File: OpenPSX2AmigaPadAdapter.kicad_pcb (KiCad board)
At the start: 2 copper layers, 58.9 x 44.2 mm, 42 parts, among them J1 TO_PSX_PAD, J2 DB9_F, J3 CONN_FTDI, J4 CONN_ICSP, J99 OSHW_LOGO, Q1 BSS138, Q2 BSS138, Q3 BSS138, Q4 BSS138, SW1 RESET, U1 ATmega328P-AU, U2 LM1117-3.3, Y1 16M, Y2 16M

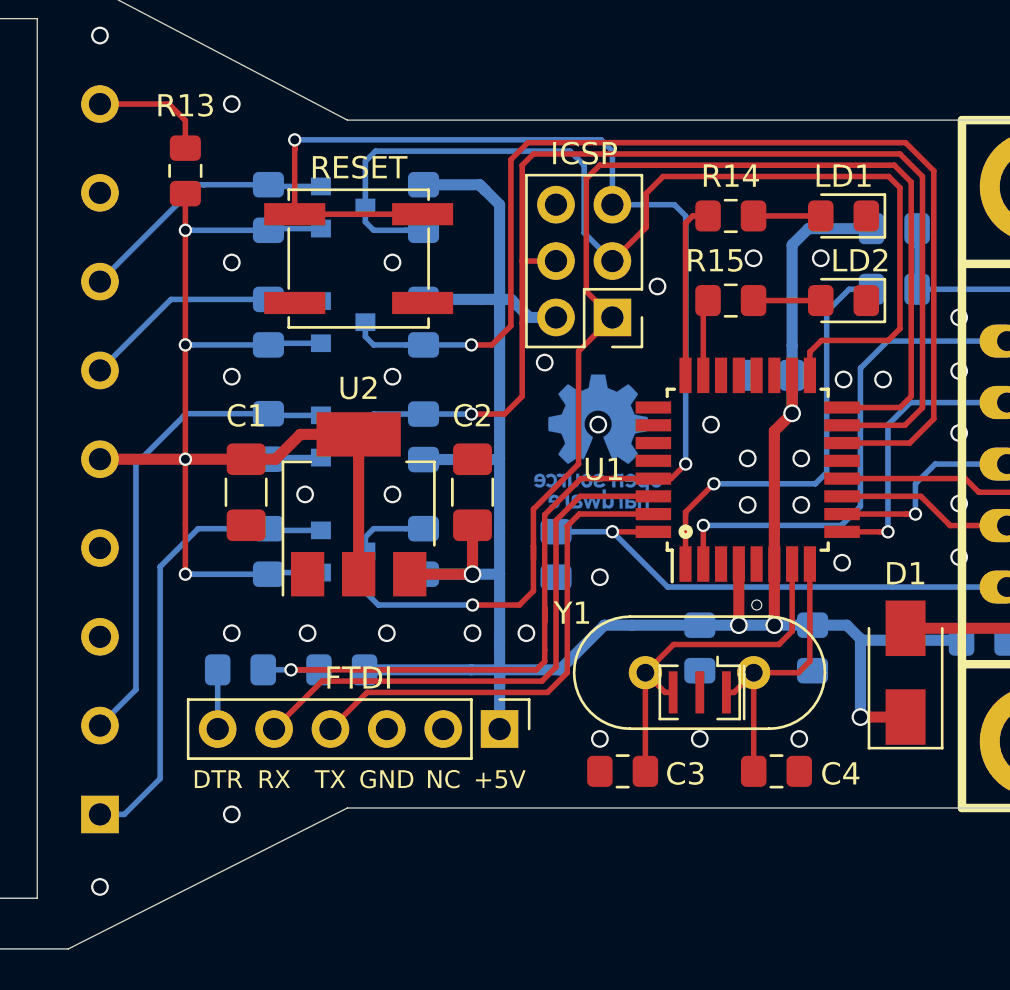
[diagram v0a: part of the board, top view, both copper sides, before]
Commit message: Use handsoldering footprints and fix FTDI connector
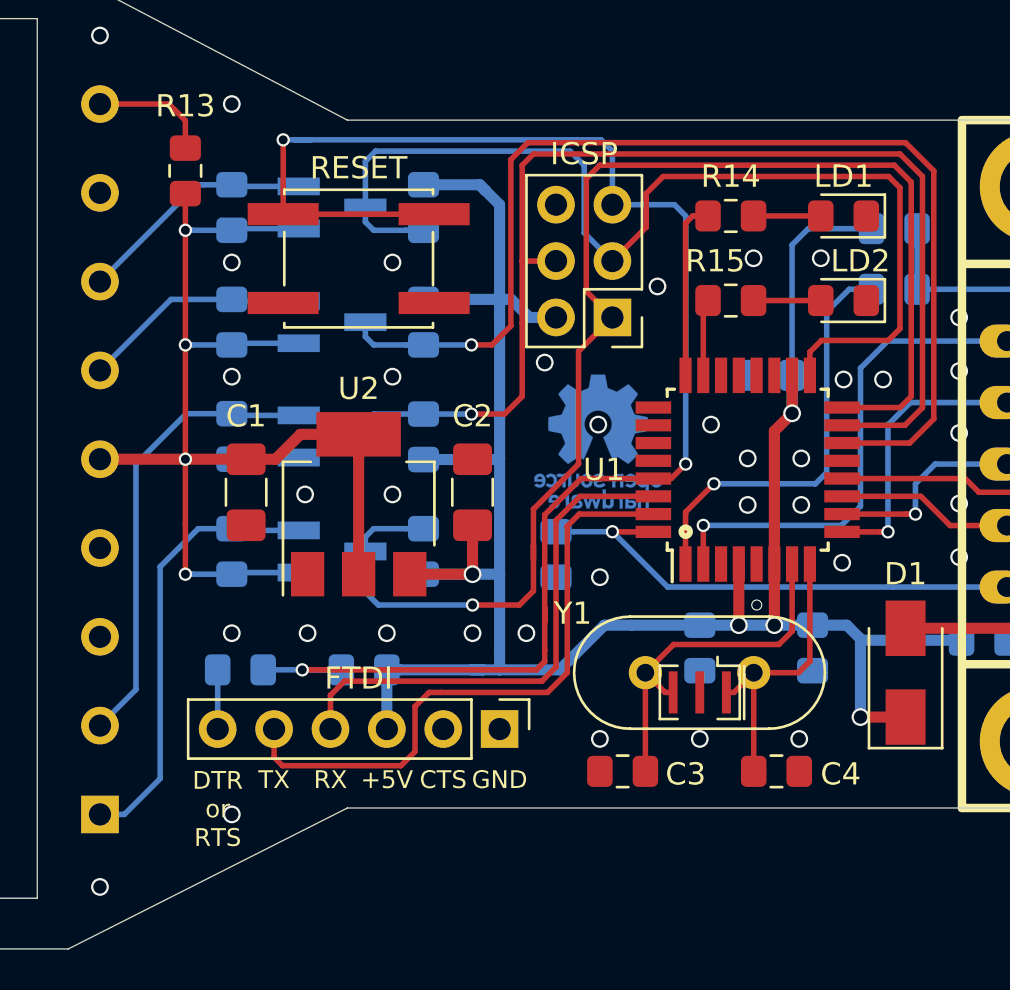
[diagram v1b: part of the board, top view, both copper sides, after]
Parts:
- removed SW1: RESET, Button_Switch_SMD:SW_SPST_EVPBF
- added SWe: RESET, Button_Switch_SMD:SW_SPST_EVQQ2, F.Cu at (128.3, 66.9)
- Q1, Q2, Q3, Q4: footprint Package_TO_SOT_SMD:SOT-23 -> Package_TO_SOT_SMD:SOT-23_Handsoldering
- moved R6 1.65 mm to (122.6, 80.1)
- moved R7 1.65 mm to (122.6, 75.0)
- moved R8 1.65 mm to (122.6, 69.8)
- moved R9 1.65 mm to (122.6, 64.6)
- moved R1 1.01 mm to (128.5, 85.5)
- moved Q1 0.50 mm to (127.1, 80.1)
- moved Q2 0.50 mm to (127.1, 75.0)
- moved Q3 0.50 mm to (127.1, 69.8)
- moved Q4 0.50 mm to (127.1, 64.6)
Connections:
- J3 pad 1: +5V -> GND
- J3 pad 2: (no net) -> GND
- J3 pad 3: GND -> +5V
- J3 pad 4: /tx -> /rx
- J3 pad 5: /rx -> /tx
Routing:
- net /tx: track 22.4 -> 28.3 mm
- net +3V3: track 60.3 -> 56.1 mm
- net /rx: track 25.3 -> 23.6 mm
- net /reset: track 69.5 -> 71.1 mm
- net /ps_cmd_3v3: track 22.0 -> 20.8 mm
- net +5V: track 106.3 -> 105.0 mm
- net /ps_attn_3v3: track 11.4 -> 10.3 mm
- net /ps_clk_3v3: track 11.9 -> 10.9 mm
- net /ps_data_3v3: track 20.9 -> 19.9 mm
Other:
- board text added: "CTS"
- board text added: "DTR or RTS"
- board text removed: "DTR"
- board text removed: "NC"

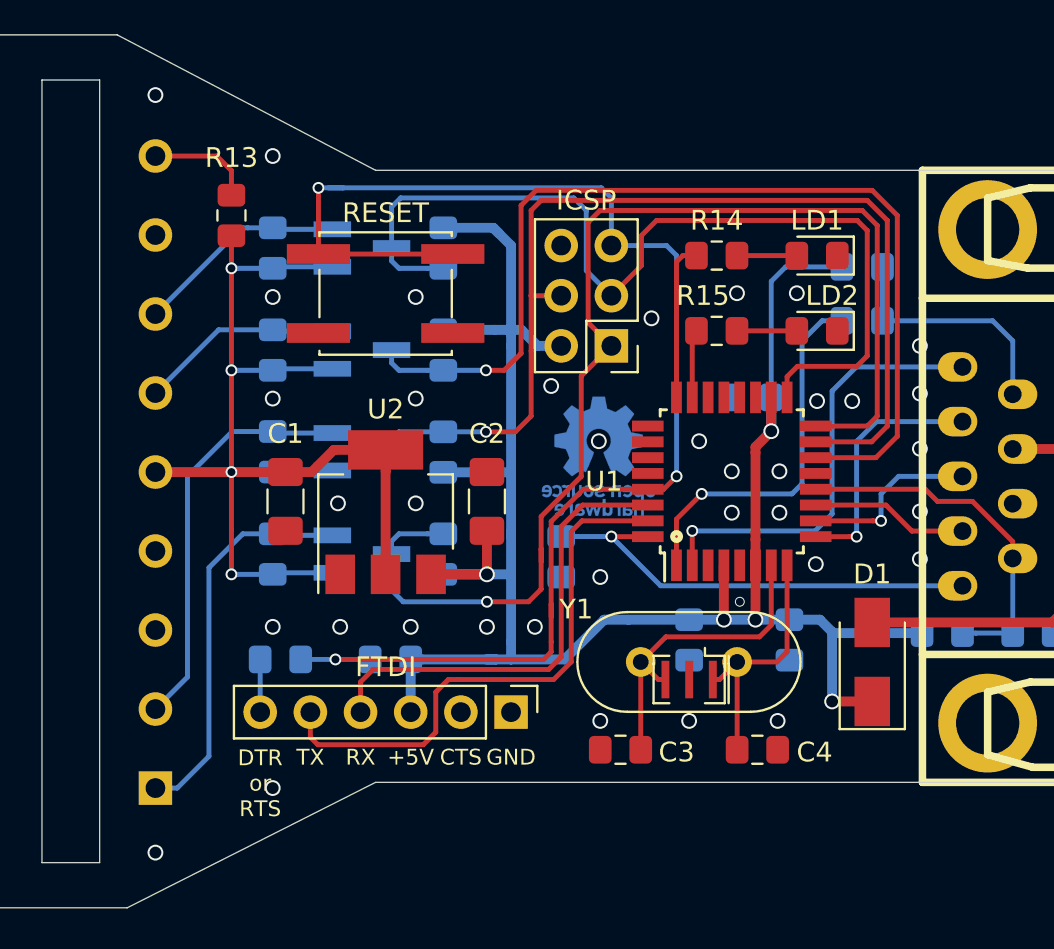
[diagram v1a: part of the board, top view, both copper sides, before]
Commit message: Connect ACK signal and remove RESET button
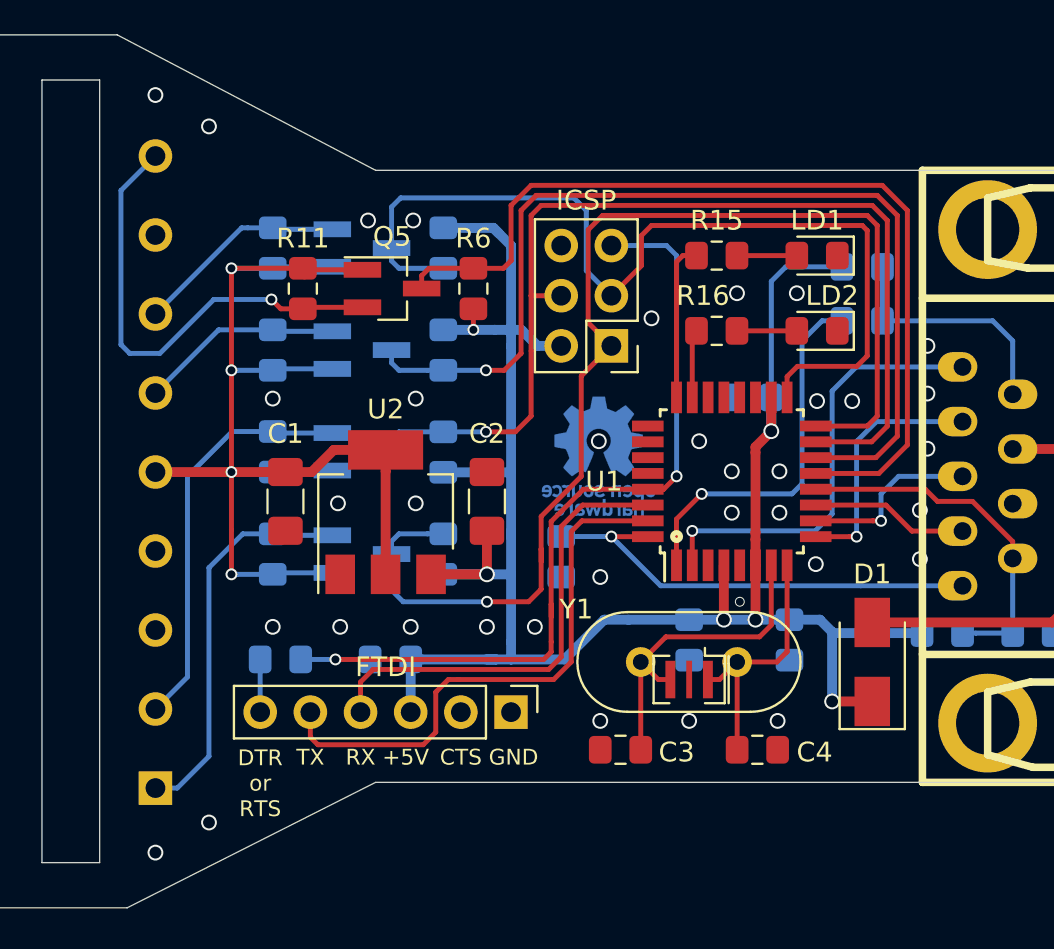
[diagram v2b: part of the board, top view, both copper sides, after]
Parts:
- removed the R13 at (120.5, 63.0)
- removed SWe: RESET, Button_Switch_SMD:SW_SPST_EVQQ2
- added Q5: BSS138, Package_TO_SOT_SMD:SOT-23_Handsoldering, F.Cu at (128.6, 66.7)
- added R11: 10k, Resistor_SMD:R_0805_2012Metric_Pad1.15x1.40mm_HandSolder, F.Cu at (124.1, 66.7)
- added R6: 10k, Resistor_SMD:R_0805_2012Metric_Pad1.15x1.40mm_HandSolder, F.Cu at (132.7, 66.7)
- Y2: footprint Crystal:Resonator_SMD_muRata_CSTxExxV-3Pin_3.0x1.1mm -> OpenPSX2AmigaPadAdapter:Resonator_SMD_muRata_CSTxExxV
- renumbered R9 to R10, R10 to R12, R11 to R13, R12 to R14, R14 to R15, R15 to R16, R6 to R7, R7 to R8, R8 to R9
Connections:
- U1 pad 13: (no net) -> /ps_ack
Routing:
- net /ps_ack: track 0.00 -> 46.4 mm
- net /reset: track 71.1 -> 43.8 mm, vias 3 -> 2
- net /ps_ack_3v3: track 5.40 -> 24.1 mm, vias 0 -> 1
- net +3V3: track 56.1 -> 61.2 mm
- net +5V: track 105.0 -> 106.1 mm, vias 5 -> 6
- net GND: vias 43 -> 42
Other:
- board text added: "V3"
- board text removed: "RESET"
- board text removed: "V2"

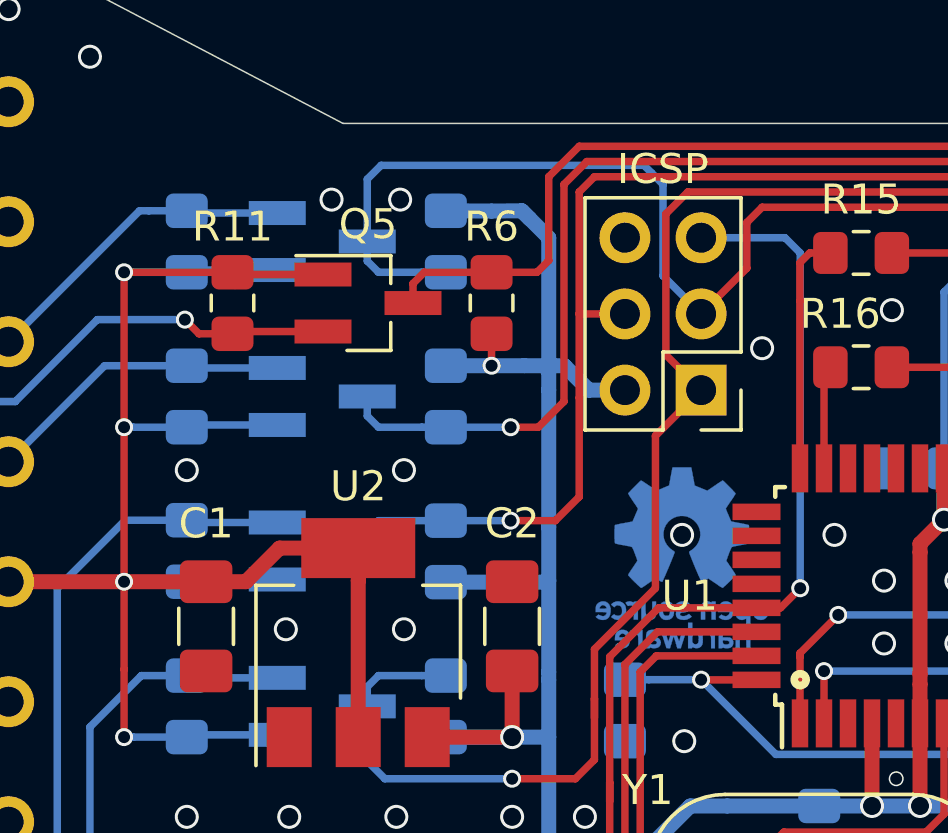
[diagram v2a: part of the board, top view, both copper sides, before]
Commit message: Fix component naming
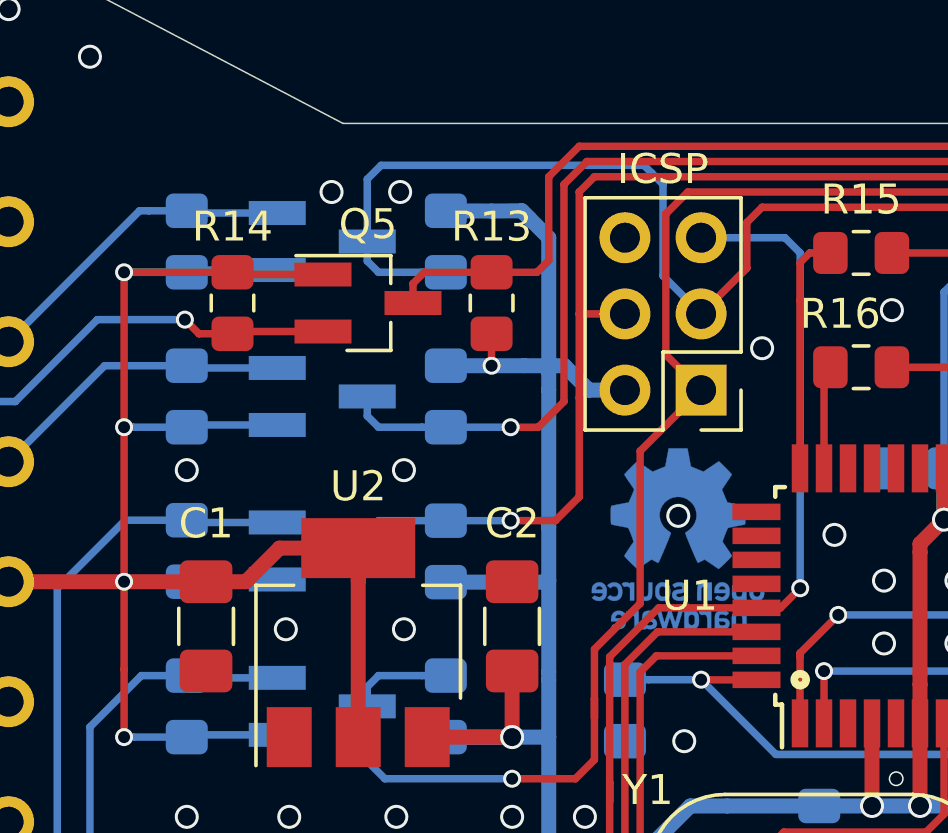
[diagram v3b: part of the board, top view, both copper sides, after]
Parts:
- moved J99 0.65 mm to (138.9, 74.5)
- renumbered R12 to R10, R13 to R11, R14 to R12, R6 to R13, R11 to R14, R7 to R6, R8 to R7, R9 to R8, R10 to R9
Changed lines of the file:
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@@
     (thickness 1.6)
     (drawings 42)
-    (tracks 390)
+    (tracks 391)
     (zones 0)
     (modules 43)
@@
   (title_block
     (title OpenPSX2AmigaPadAdapter)
-    (date 2019-12-17)
+    (date 2020-01-02)
     (rev 3)
     (company SukkoPera)
@@
   (net 30 "Net-(C4-Pad2)")
   (net 31 /ps_ack)
-  (net 32 "Net-(R12-Pad2)")
+  (net 32 "Net-(R10-Pad2)")
   (net_class Default "This is the default net class."
     (clearance 0.2)
@@
     (add_net "Net-(LD1-Pad2)")
     (add_net "Net-(LD2-Pad2)")
-    (add_net "Net-(R12-Pad2)")
+    (add_net "Net-(R10-Pad2)")
   )
   (net_class Power ""
@@
     (tags "resistor handsolder")
     (attr smd)
-    (fp_text reference R7 (at -2.5 0) (layer B.SilkS)
+    (fp_text reference R6 (at -2.5 0) (layer B.SilkS)
       (effects (font (size 1 1) (thickness 0.15)) (justify mirror))
     )
@@
     (tags "resistor handsolder")
     (attr smd)
-    (fp_text reference R8 (at -2.5 0) (layer B.SilkS)
+    (fp_text reference R7 (at -2.5 0) (layer B.SilkS)
       (effects (font (size 1 1) (thickness 0.15)) (justify mirror))
     )
@@
     (tags "resistor handsolder")
     (attr smd)
-    (fp_text reference R9 (at -2.5 0) (layer B.SilkS)
+    (fp_text reference R8 (at -2.5 0) (layer B.SilkS)
       (effects (font (size 1 1) (thickness 0.15)) (justify mirror))
     )
@@
     (tags "resistor handsolder")
     (attr smd)
-    (fp_text reference R10 (at -2.5 0.254) (layer B.SilkS)
+    (fp_text reference R9 (at -2.5 0.254) (layer B.SilkS)
       (effects (font (size 1 1) (thickness 0.15)) (justify mirror))
     )
@@
     (tags "resistor handsolder")
     (attr smd)
-    (fp_text reference R12 (at 3.556 0) (layer B.SilkS)
+    (fp_text reference R10 (at 3.556 0) (layer B.SilkS)
       (effects (font (size 1 1) (thickness 0.15)) (justify mirror))
     )
@@
     (fp_line (start -1 -0.6) (end -1 0.6) (layer B.Fab) (width 0.1))
     (pad 2 smd roundrect (at 1.025 0 180) (size 1.15 1.4) (layers B.Cu B.Paste B.Mask) (roundrect_rratio 0.217391)
-      (net 32 "Net-(R12-Pad2)"))
+      (net 32 "Net-(R10-Pad2)"))
     (pad 1 smd roundrect (at -1.025 0 180) (size 1.15 1.4) (layers B.Cu B.Paste B.Mask) (roundrect_rratio 0.217391)
       (net 17 /ami_fire))
@@
     (fp_line (start -3.625 -3.4) (end -5.05 -3.4) (layer F.SilkS) (width 0.15))
     (pad 1 smd rect (at -4.25 -2.8 90) (size 1.6 0.55) (layers F.Cu F.Paste F.Mask)
-      (net 32 "Net-(R12-Pad2)"))
+      (net 32 "Net-(R10-Pad2)"))
     (pad 2 smd rect (at -4.25 -2 90) (size 1.6 0.55) (layers F.Cu F.Paste F.Mask)
       (net 13 /ami_up))
@@
   )
   (module Symbol:OSHW-Logo_5.7x6mm_Copper (layer B.Cu)
-    (at 139.065 75.184 180)
+    (at 138.938 74.549 180)
     (descr "Open Source Hardware Logo")
     (tags "Logo OSHW")
@@
     (tags "resistor handsolder")
     (attr smd)
-    (fp_text reference R14 (at -3.547 0.0635) (layer B.SilkS)
+    (fp_text reference R12 (at -3.547 0.0635) (layer B.SilkS)
       (effects (font (size 1 1) (thickness 0.15)) (justify mirror))
     )
@@
     (tags "resistor handsolder")
     (attr smd)
-    (fp_text reference R13 (at -3.556 0) (layer B.SilkS)
+    (fp_text reference R11 (at -3.556 0) (layer B.SilkS)
       (effects (font (size 1 1) (thickness 0.15)) (justify mirror))
     )
@@
     (tags "resistor handsolder")
     (attr smd)
-    (fp_text reference R6 (at 2.542999 0 180) (layer F.SilkS)
+    (fp_text reference R13 (at 2.542999 0 180) (layer F.SilkS)
       (effects (font (size 1 1) (thickness 0.15)))
     )
@@
     (tags "resistor handsolder")
     (attr smd)
-    (fp_text reference R11 (at -2.542999 0 180) (layer F.SilkS)
+    (fp_text reference R14 (at -2.542999 0 180) (layer F.SilkS)
       (effects (font (size 1 1) (thickness 0.15)))
     )
@@
   (via (at 139.137 88.5825) (size 0.8) (drill 0.6) (layers F.Cu B.Cu) (net 1))
   (via (at 139.137 81.298) (size 0.8) (drill 0.6) (layers F.Cu B.Cu) (net 1))
-  (via (at 139.065 74.422) (size 0.8) (drill 0.6) (layers F.Cu B.Cu) (net 1))
+  (via (at 138.938 73.787) (size 0.8) (drill 0.6) (layers F.Cu B.Cu) (net 1))
   (via (at 141.732 68.199) (size 0.8) (drill 0.6) (layers F.Cu B.Cu) (net 1))
   (via (at 122.555 83.82) (size 0.8) (drill 0.6) (layers F.Cu B.Cu) (net 1))
@@
   (via (at 116.616 56.896) (size 0.8) (drill 0.6) (layers F.Cu B.Cu) (net 1))
   (via (at 149.089 66.929) (size 0.8) (drill 0.6) (layers F.Cu B.Cu) (net 1))
-  (via (at 129.667 63.246) (size 0.8) (drill 0.6) (layers F.Cu B.Cu) (net 1))
-  (via (at 127.381 63.246) (size 0.8) (drill 0.6) (layers F.Cu B.Cu) (net 1))
+  (via (at 129.667 62.992) (size 0.8) (drill 0.6) (layers F.Cu B.Cu) (net 1))
+  (via (at 127.381 62.992) (size 0.8) (drill 0.6) (layers F.Cu B.Cu) (net 1))
   (via (at 119.32725 58.4835) (size 0.8) (drill 0.6) (layers F.Cu B.Cu) (net 1))
   (segment (start 146.996 79.404) (end 146.996 80.704) (width 0.5) (layer F.Cu) (net 2) (status 20))
@@
   (segment (start 128.5715 80.137) (end 128.5715 81.9625) (width 0.25) (layer B.Cu) (net 20) (status 10))
   (segment (start 136.144 78.232) (end 136.144 79.883) (width 0.25) (layer F.Cu) (net 20))
-  (segment (start 138.176 76.2) (end 136.144 78.232) (width 0.25) (layer F.Cu) (net 20))
-  (segment (start 138.176 71.12) (end 138.176 76.2) (width 0.25) (layer F.Cu) (net 20))
-  (segment (start 139.7 69.596) (end 138.176 71.12) (width 0.25) (layer F.Cu) (net 20) (status 10))
   (segment (start 152.66 73.654) (end 150.046 73.654) (width 0.25) (layer F.Cu) (net 20) (status 20))
   (segment (start 153.162 73.152) (end 152.66 73.654) (width 0.25) (layer F.Cu) (net 20))
@@
   (segment (start 138.524999 63.721999) (end 139.254998 62.992) (width 0.25) (layer F.Cu) (net 20))
   (segment (start 152.654 62.992) (end 153.162 63.5) (width 0.25) (layer F.Cu) (net 20))
+  (segment (start 137.668 76.708) (end 137.668 71.628) (width 0.25) (layer F.Cu) (net 20))
+  (segment (start 137.668 76.708) (end 136.144 78.232) (width 0.25) (layer F.Cu) (net 20))
+  (segment (start 137.668 71.628) (end 138.557 70.739) (width 0.25) (layer F.Cu) (net 20))
+  (segment (start 139.7 69.596) (end 138.557 70.739) (width 0.25) (layer F.Cu) (net 20))
   (segment (start 128.9465 65.668) (end 130.391 65.668) (width 0.25) (layer B.Cu) (net 21))
   (segment (start 130.391 65.668) (end 131.191 65.668) (width 0.25) (layer B.Cu) (net 21) (status 20))
@@
   (via (at 122.4915 67.2465) (size 0.6) (drill 0.4) (layers F.Cu B.Cu) (net 28))
   (segment (start 122.963 67.718) (end 122.4915 67.2465) (width 0.25) (layer F.Cu) (net 28))
-  (segment (start 124.079 67.718) (end 122.963 67.718) (width 0.25) (layer F.Cu) (net 28))
+  (segment (start 124.079 67.718) (end 122.963 67.718) (width 0.25) (layer F.Cu) (net 28) (status 10))
   (segment (start 119.5705 67.2465) (end 122.4915 67.2465) (width 0.25) (layer B.Cu) (net 28))
   (segment (start 116.84 69.977) (end 119.5705 67.2465) (width 0.25) (layer B.Cu) (net 28))
@@
   (segment (start 114.8715 61.727) (end 114.8715 69.5325) (width 0.25) (layer B.Cu) (net 28))
   (segment (start 115.316 69.977) (end 116.84 69.977) (width 0.25) (layer B.Cu) (net 28))
-  (segment (start 116.616 59.9825) (end 114.8715 61.727) (width 0.25) (layer B.Cu) (net 28))
+  (segment (start 116.616 59.9825) (end 114.8715 61.727) (width 0.25) (layer B.Cu) (net 28) (status 10))
   (segment (start 141.187 85.598) (end 141.187 89.916) (width 0.25) (layer F.Cu) (net 29) (status 30))
   (segment (start 142.457 84.328) (end 141.187 85.598) (width 0.25) (layer F.Cu) (net 29) (status 20))
@@
   (segment (start 147.796 80.704) (end 147.796 83.731002) (width 0.25) (layer F.Cu) (net 29) (status 10))
   (segment (start 142.076 86.487) (end 141.187 85.598) (width 0.25) (layer F.Cu) (net 29) (status 20))
-  (segment (start 142.076 86.487) (end 142.687 86.487) (width 0.25) (layer F.Cu) (net 29))
+  (segment (start 142.076 86.487) (end 142.687 86.487) (width 0.25) (layer F.Cu) (net 29) (status 20))
   (segment (start 146.067 85.598) (end 146.067 89.916) (width 0.25) (layer F.Cu) (net 30) (status 30))
   (segment (start 148.596 85.084) (end 148.082 85.598) (width 0.25) (layer F.Cu) (net 30))
@@
   (segment (start 148.596 80.704) (end 148.596 85.084) (width 0.25) (layer F.Cu) (net 30) (status 10))
   (segment (start 145.178 86.487) (end 146.067 85.598) (width 0.25) (layer F.Cu) (net 30) (status 20))
-  (segment (start 145.178 86.487) (end 144.587 86.487) (width 0.25) (layer F.Cu) (net 30))
+  (segment (start 145.178 86.487) (end 144.587 86.487) (width 0.25) (layer F.Cu) (net 30) (status 20))
   (segment (start 130.0955 66.043) (end 130.0955 66.693) (width 0.25) (layer F.Cu) (net 31) (status 20))
   (segment (start 130.4705 65.668) (end 130.0955 66.043) (width 0.25) (layer F.Cu) (net 31))
